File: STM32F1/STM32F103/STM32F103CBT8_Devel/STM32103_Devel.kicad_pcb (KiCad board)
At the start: 4 copper layers, 69 x 50 mm, 46 parts, among them J1 Conn_02x03_Odd_Even, J2 USB_B_Micro, J3 Conn_02x10_Odd_Even, J4 Conn_01x16, J5 Conn_01x16, J6 Conn_02x05 Odd_Even, SW1 SW_Push, U1 STM32F103CBTx, U2 AMS1117-3.3, Y1 8MHz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

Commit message: Kicad Reorg
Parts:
- C10: value CP -> 10uf
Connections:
- net /BOOT0 renamed /STM32F103CB/BOOT0
- net /BOOT1 renamed /PB2
- net /OSC32_IN renamed /STM32F103CB/PC15
- net /OSC32_OUT renamed /STM32F103CB/PC14
- net /OSC_IN renamed /STM32F103CB/PD0
- net /OSC_OUT renamed /STM32F103CB/PD1
- net /PC13 renamed /STM32F103CB/PC13
- net /RST renamed /STM32F103CB/NRST
- net /USB_N renamed /USB/USB_N
- net /USB_P renamed /USB/USB_P

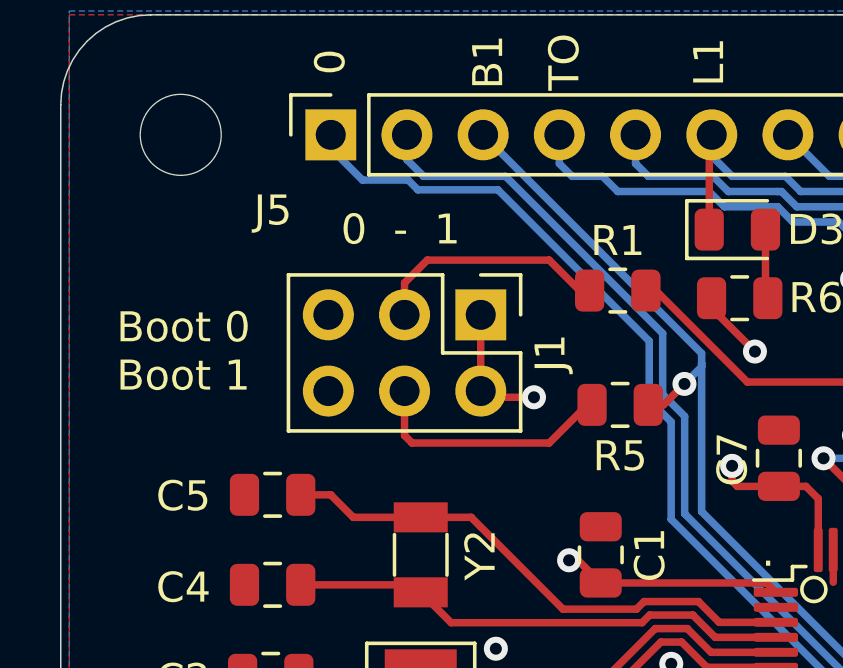
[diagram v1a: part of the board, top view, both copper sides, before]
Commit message: Update to dip sw and local VCC
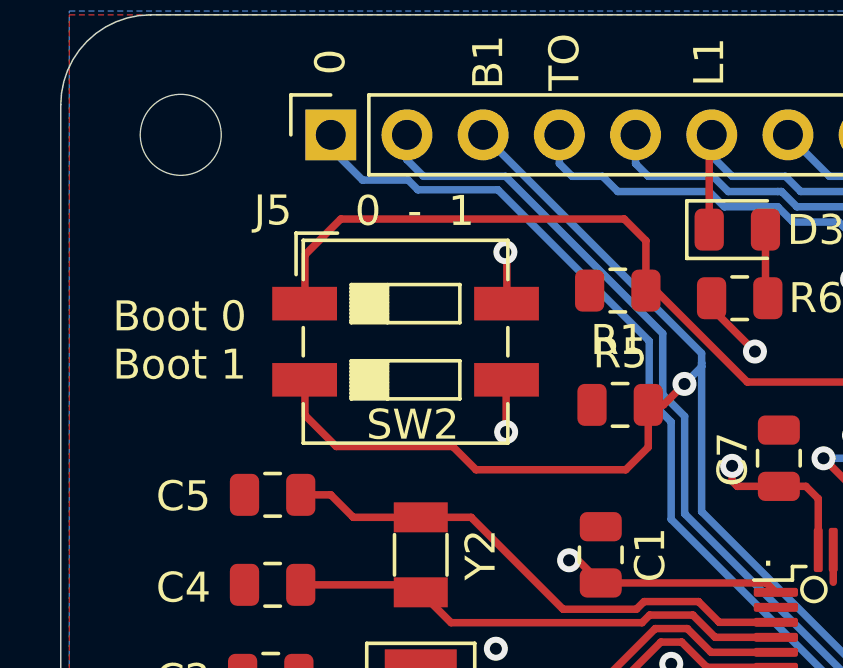
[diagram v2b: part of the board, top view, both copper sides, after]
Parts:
- removed J1: Conn_02x03_Odd_Even, Connector_PinHeader_2.54mm:PinHeader_2x03_P2.54mm_Vertical
- added SW2: SW_DIP_x02, Button_Switch_SMD:SW_DIP_SPSTx02_Slide_6.7x6.64mm_W6.73mm_P2.54mm_LowProfile_JPin, F.Cu at (111.5, 80.9)
- turned R1 to 180 degrees
- turned R5 to 180 degrees
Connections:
- net VDDA renamed /STM32F103CB/_VDDA
- R1 pad 1: Net-(J1-Pad3) -> /STM32F103CB/BOOT0
- R1 pad 2: /STM32F103CB/BOOT0 -> GND
- R5 pad 1: Net-(J1-Pad4) -> /PB2
- R5 pad 2: /PB2 -> GND
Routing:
- net /STM32F103CB/BOOT0: track 14.1 -> 29.6 mm
- net /PB2: track 35.0 -> 50.0 mm
- net Net-(J1-Pad4): track 8.36 -> 0.00 mm
- net Net-(J1-Pad3): track 7.97 -> 0.00 mm
- net VCC: track 58.5 -> 57.6 mm, vias 11 -> 12

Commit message: StmF103 updated to kicad8 and kibot
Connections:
- net /STM32F103CB/NRST renamed /STM32F103CB/RST
- net /STM32F103CB/PC14 renamed /STM32F103CB/OSC32_OUT
- net /STM32F103CB/PC15 renamed /STM32F103CB/OSC32_IN
- net /STM32F103CB/PD0 renamed /STM32F103CB/OSC_IN
- net /STM32F103CB/PD1 renamed /STM32F103CB/OSC_OUT
- D4 pad 2: Net-(D4-Pad2) -> (no net)
- J2 pad 1: Net-(D4-Pad2) -> (no net)
- J2 pad 4: Net-(J2-Pad4) -> (no net)
- J3 pad 11: Net-(J3-Pad11) -> unconnected-(J3-Pin_11-Pad11)
- J3 pad 17: Net-(J3-Pad17) -> unconnected-(J3-Pin_17-Pad17)
- J3 pad 19: Net-(J3-Pad19) -> unconnected-(J3-Pin_19-Pad19)
- J3 pad 3: Net-(J3-Pad3) -> unconnected-(J3-Pin_3-Pad3)
- J3 pad 5: Net-(J3-Pad5) -> unconnected-(J3-Pin_5-Pad5)
- J6 pad 7: Net-(J6-Pad7) -> unconnected-(J6-Pin_7-Pad7)
- J6 pad 8: Net-(J6-Pad8) -> unconnected-(J6-Pin_8-Pad8)
- R7 pad 1: Net-(J2-Pad4) -> (no net)
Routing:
- net (no net): track 0.00 -> 20.3 mm
- net Net-(D4-Pad2): track 15.4 -> 0.00 mm
- net Net-(J2-Pad4): track 4.86 -> 0.00 mm
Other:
- net class 5V removed
- net class Default removed

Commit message: Mpn ids
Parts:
- Y2: value Crystal -> 32.768kHz

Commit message: Mov USB
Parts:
- removed J3: Conn_02x10_Odd_Even, Connector_PinHeader_2.54mm:PinHeader_2x10_P2.54mm_Vertical
- H1, H2, H3, H4: footprint MountingHole:MountingHole_2.7mm_M2.5 -> MountingHole:MountingHole_2.7mm_M2.5_DIN965_Pad
- J6: footprint Connector_PinHeader_1.27mm:PinHeader_2x05_P1.27mm_Vertical -> Connector_PinHeader_1.27mm:PinHeader_2x05_P1.27mm_Vertical_SMD
- moved J6 21.8 mm to (164.0, 103.0), turned to 180 degrees
- moved J2 15.1 mm to (165.2, 86.0), turned to 90 degrees
- moved R7 8.94 mm to (160.5, 82.6), turned to 90 degrees
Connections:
- D4 pad 2: (no net) -> /USB/VCC_USB
- J2 pad 1: (no net) -> /USB/VCC_USB
- J2 pad 4: (no net) -> unconnected-(J2-ID-Pad4)
- R7 pad 1: (no net) -> unconnected-(J2-ID-Pad4)
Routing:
- net (no net): track 20.3 -> 0.00 mm
- net /STM32F103CB/RST: track 97.1 -> 77.5 mm, vias 3 -> 2
- net /USB/VCC_USB: track 0.00 -> 11.6 mm
- net /PB3: track 79.8 -> 73.5 mm
- net /PA14: track 88.5 -> 83.1 mm
- net /USB/USB_P: track 16.8 -> 21.4 mm
- net unconnected-(J2-ID-Pad4): track 0.00 -> 4.20 mm
- net /USB/USB_N: track 15.5 -> 19.3 mm
- net VCC: track 57.6 -> 60.1 mm, vias 12 -> 13
- net GND: track 5.35 -> 4.39 mm, vias 4 -> 2

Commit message: Silk Changes
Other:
- board text added: "CAN_RX CAN_TX"
- board text added: "MOSI1 MISO1 SCK1"
- board text added: "OI I0 SC"
- board text added: "RX1 TX1"
- board text added: "RX2 TX2"
- board text added: "SC SD"
- board text added: "SCK1 MISO1 MOSI1"
- board text added: "SCK2 MISO2 MOSI2"
- board text added: "SCL1 SDA1"
- board text added: "SCL2 TX3 SDA2 RX3"
- board text added: "SDA2 RX3 SCL2 TX3"
- board text added: "TX1 RX1"
- board text added: "TX2 RX2"
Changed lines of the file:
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@@
 		)
 		(property "Value" "8MHz"
-			(at 0 2.8 90)
+			(at 1.5 -2.5 90)
 			(layer "F.Fab")
 			(effects
@@
 		)
 		(property "Value" "1K"
-			(at 0 1.65 0)
+			(at 2.868 0.054 0)
 			(layer "F.Fab")
 			(effects
@@
 		)
 		(property "Value" "32.768kHz"
-			(at 0 2 90)
+			(at -2.5 -2.5 180)
 			(layer "F.Fab")
 			(effects
@@
 		)
 		(property "Value" "1uF"
-			(at 0 1.65 90)
+			(at -3.1995 0.326 90)
 			(layer "F.Fab")
 			(effects
@@
 		)
 		(property "Value" "10pf"
-			(at 0 1.65 0)
+			(at 3.5625 0 0)
 			(layer "F.Fab")
 			(effects
@@
 		)
 		(property "Value" "100nf"
-			(at 0 1.65 90)
+			(at 0 -2 90)
 			(layer "F.Fab")
 			(effects
@@
 		)
 		(property "Value" "100nf"
-			(at 0 1.65 0)
+			(at 0 -1.734 0)
 			(layer "F.Fab")
 			(effects
@@
 		)
 		(property "Value" "1uF"
-			(at 0 1.65 90)
+			(at -3.262 0.124 90)
 			(layer "F.Fab")
 			(effects
@@
 		)
 		(property "Value" "100K"
-			(at 0 1.65 90)
+			(at 0.0625 -1.5 90)
 			(layer "F.Fab")
 			(effects
@@
 		)
 		(property "Value" "10K"
-			(at 0 1.65 90)
+			(at -0.0625 -2 90)
 			(layer "F.Fab")
 			(effects
@@
 		)
 		(property "Value" "1K"
-			(at 0 1.65 90)
+			(at -0.0625 -2 90)
 			(layer "F.Fab")
 			(effects
@@
 		)
 		(property "Value" "AMS1117-3.3"
-			(at 0 4.5 90)
+			(at 3 -2 180)
 			(layer "F.Fab")
 			(effects
@@
 		)
 		(property "Value" "20pf"
-			(at 0 1.65 0)
+			(at 3.5625 0 0)
 			(layer "F.Fab")
 			(effects
@@
 		)
 		(property "Value" "GREEN"
-			(at 0 1.65 0)
+			(at 4.4465 -0.16 0)
 			(layer "F.Fab")
 			(effects
@@
 		)
 		(property "Value" "20"
-			(at 0 1.65 0)
+			(at 2.746 0.03 0)
 			(layer "F.Fab")
 			(effects
@@
 		)
 		(property "Value" "10nF"
-			(at 0 1.65 90)
+			(at -3.762 0.338 90)
 			(layer "F.Fab")
 			(effects
@@
 		)
 		(property "Value" "STM32F103CBTx"
-			(at 0 5.85 0)
+			(at 1 2 0)
 			(layer "F.Fab")
 			(effects
@@
 		)
 		(property "Value" "10pf"
-			(at 0 1.65 0)
+			(at 3.5625 0 0)
 			(layer "F.Fab")
 			(effects
@@
 		)
 		(property "Value" "20pf"
-			(at 0 1.65 0)
+			(at 3.5 0 0)
 			(layer "F.Fab")
 			(effects
@@
 		)
 		(property "Value" "100nf"
-			(at 0 1.65 90)
+			(at 0 -2 90)
 			(layer "F.Fab")
 			(effects
@@
 		)
 		(property "Value" "10uf"
-			(at 0 1.75 0)
+			(at 4 0 0)
 			(layer "F.Fab")
 			(effects
@@
 		)
 		(property "Value" "1K5"
-			(at 0 1.65 0)
+			(at -3.216 -0.11 0)
 			(layer "F.Fab")
 			(effects
@@
 		)
 		(property "Value" "10nF"
-			(at 0 1.65 90)
+			(at -3.694 0.202 90)
 			(layer "F.Fab")
 			(effects
@@
 		)
 		(property "Value" "20"
-			(at 0 1.65 0)
+			(at -2.746 0.016 0)
 			(layer "F.Fab")
 			(effects
@@
 		)
 		(property "Value" "Conn_01x16"
-			(at 0 40.87 90)
+			(at 2.5 31.5 180)
 			(layer "F.Fab")
 			(effects
@@
 		)
 		(fp_text user "${REFERENCE}"
-			(at 0 19.05 0)
+			(at 2.5 19.05 0)
 			(layer "F.Fab")
 			(effects
@@
 		)
 		(property "Value" "Conn_01x16"
-			(at 0 40.87 90)
+			(at -2.5 24 180)
 			(layer "F.Fab")
 			(effects
@@
 		)
 		(fp_text user "${REFERENCE}"
-			(at 0 19.05 0)
+			(at 2.5 19.5 0)
 			(layer "F.Fab")
 			(effects
@@
 		)
 		(property "Value" "SW_DIP_x02"
-			(at 0 4.38 0)
+			(at -8.9935 -2.3967 0)
 			(layer "F.Fab")
 			(effects
@@
 		(layer "Margin")
 	)
+	(gr_text "SCK2\nMISO2\nMOSI2"
+		(at 147 75.5 90)
+		(layer "B.SilkS")
+		(effects
+			(font
+				(size 1 1)
+				(thickness 0.15)
+			)
+			(justify left bottom mirror)
+		)
+	)
+	(gr_text "SCL1\nSDA1"
+		(at 127 75.5 90)
+		(layer "B.SilkS")
+		(effects
+			(font
+				(size 1 1)
+				(thickness 0.15)
+			)
+			(justify left bottom mirror)
+		)
+	)
+	(gr_text "RX1\nTX1\n"
+		(at 131.5 114.5 270)
+		(layer "B.SilkS")
+		(effects
+			(font
+				(size 1 1)
+				(thickness 0.15)
+			)
+			(justify left bottom mirror)
+		)
+	)
+	(gr_text "SCL2 TX3\nSDA2 RX3"
+		(at 137 75.5 90)
+		(layer "B.SilkS")
+		(effects
+			(font
+				(size 1 1)
+				(thickness 0.15)
+			)
+			(justify left bottom mirror)
+		)
+	)
+	(gr_text "MOSI1\nMISO1\nSCK1"
+		(at 122 114.5 -90)
+		(layer "B.SilkS")
+		(effects
+			(font
+				(size 1 1)
+				(thickness 0.15)
+			)
+			(justify left bottom mirror)
+		)
+	)
+	(gr_text "CAN_RX\nCAN_TX"
+		(at 132 75.5 90)
+		(layer "B.SilkS")
+		(effects
+			(font
+				(size 1 1)
+				(thickness 0.15)
+			)
+			(justify left bottom mirror)
+		)
+	)
+	(gr_text "RX2\nTX2\n"
+		(at 114 114.5 270)
+		(layer "B.SilkS")
+		(effects
+			(font
+				(size 1 1)
+				(thickness 0.15)
+			)
+			(justify left bottom mirror)
+		)
+	)
 	(gr_text "0  -  1"
 		(at 111.7983 76.5406 0)
@@
 	)
 	(gr_text "PB"
-		(at 127.966 71.318 0)
+		(at 131 71.318 0)
 		(layer "F.SilkS")
 		(effects
@@
 		)
 	)
+	(gr_text "TX2\nRX2"
+		(at 117 114.5 90)
+		(layer "F.SilkS")
+		(effects
+			(font
+				(size 1 1)
+				(thickness 0.15)
+			)
+			(justify left bottom)
+		)
+	)
+	(gr_text "SCK1\nMISO1\nMOSI1"
+		(at 126.5 114.5 90)
+		(layer "F.SilkS")
+		(effects
+			(font
+				(size 1 1)
+				(thickness 0.15)
+			)
+			(justify left bottom)
+		)
+	)
+	(gr_text "SDA2 RX3\nSCL2 TX3"
+		(at 134 75.5 270)
+		(layer "F.SilkS")
+		(effects
+			(font
+				(size 1 1)
+				(thickness 0.15)
+			)
+			(justify left bottom)
+		)
+	)
 	(gr_text "-3.3V"
 		(at 143.523 94.051 90)
@@
 		)
 	)
+	(gr_text "OI\nI0\nSC"
+		(at 142.5 76 270)
+		(layer "F.SilkS")
+		(effects
+			(font
+				(size 1 1)
+				(thickness 0.15)
+			)
+			(justify left bottom)
+		)
+	)
 	(gr_text "-5V"
 		(at 137.3 94.813 90)
@@
 		)
 	)
+	(gr_text "TX1\nRX1"
+		(at 134.5 114.5 90)
+		(layer "F.SilkS")
+		(effects
+			(font
+				(size 1 1)
+				(thickness 0.15)
+			)
+			(justify left bottom)
+		)
+	)
+	(gr_text "SC\nSD"
+		(at 127 72.5 90)
+		(layer "F.SilkS")
+		(effects
+			(font
+				(size 1 1)
+				(thickness 0.15)
+			)
+			(justify left bottom)
+		)
+	)
